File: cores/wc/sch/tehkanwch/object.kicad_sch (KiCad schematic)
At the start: 4 parts

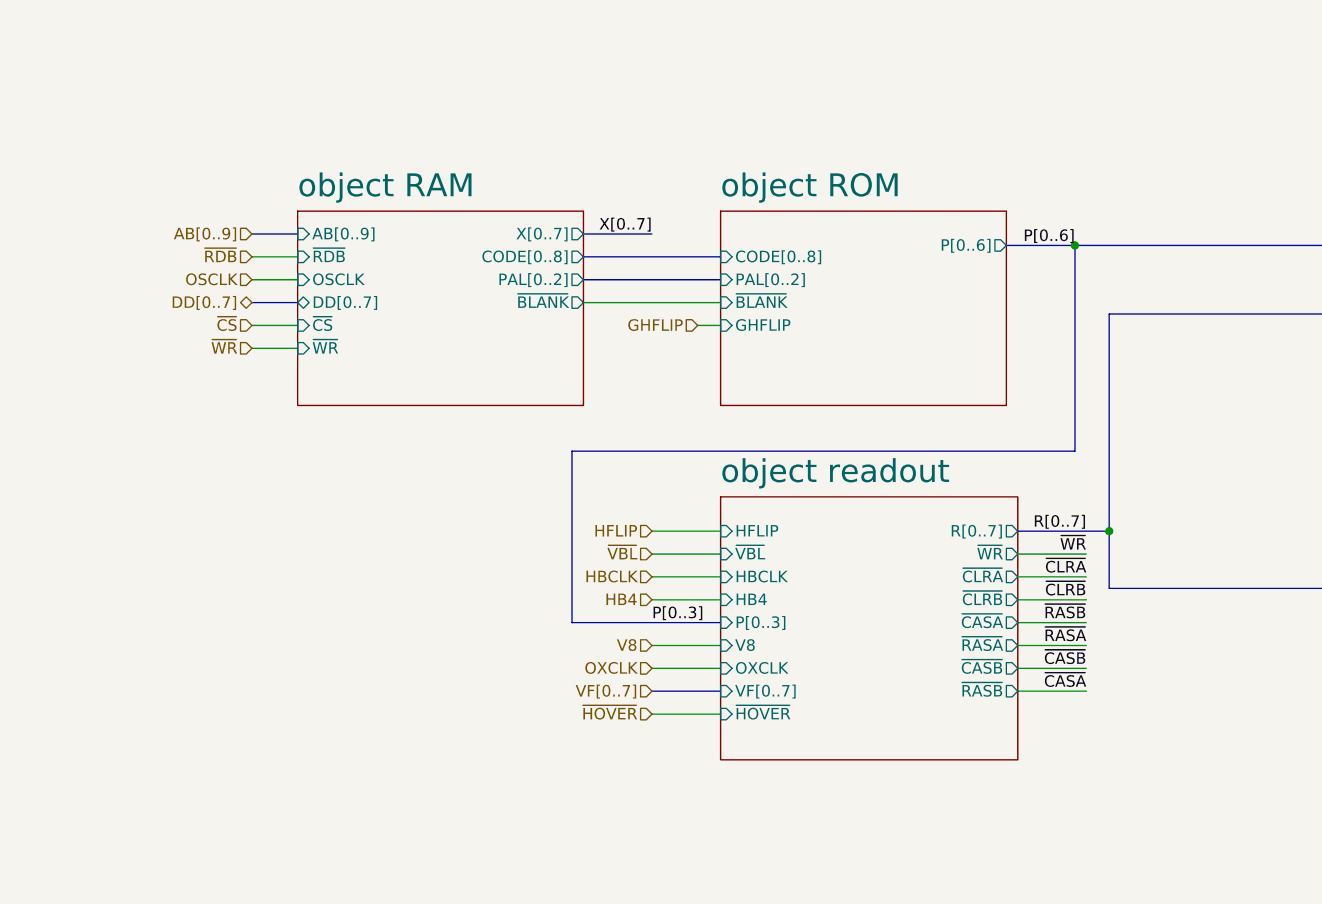
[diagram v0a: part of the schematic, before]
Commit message: wc: all modules connected
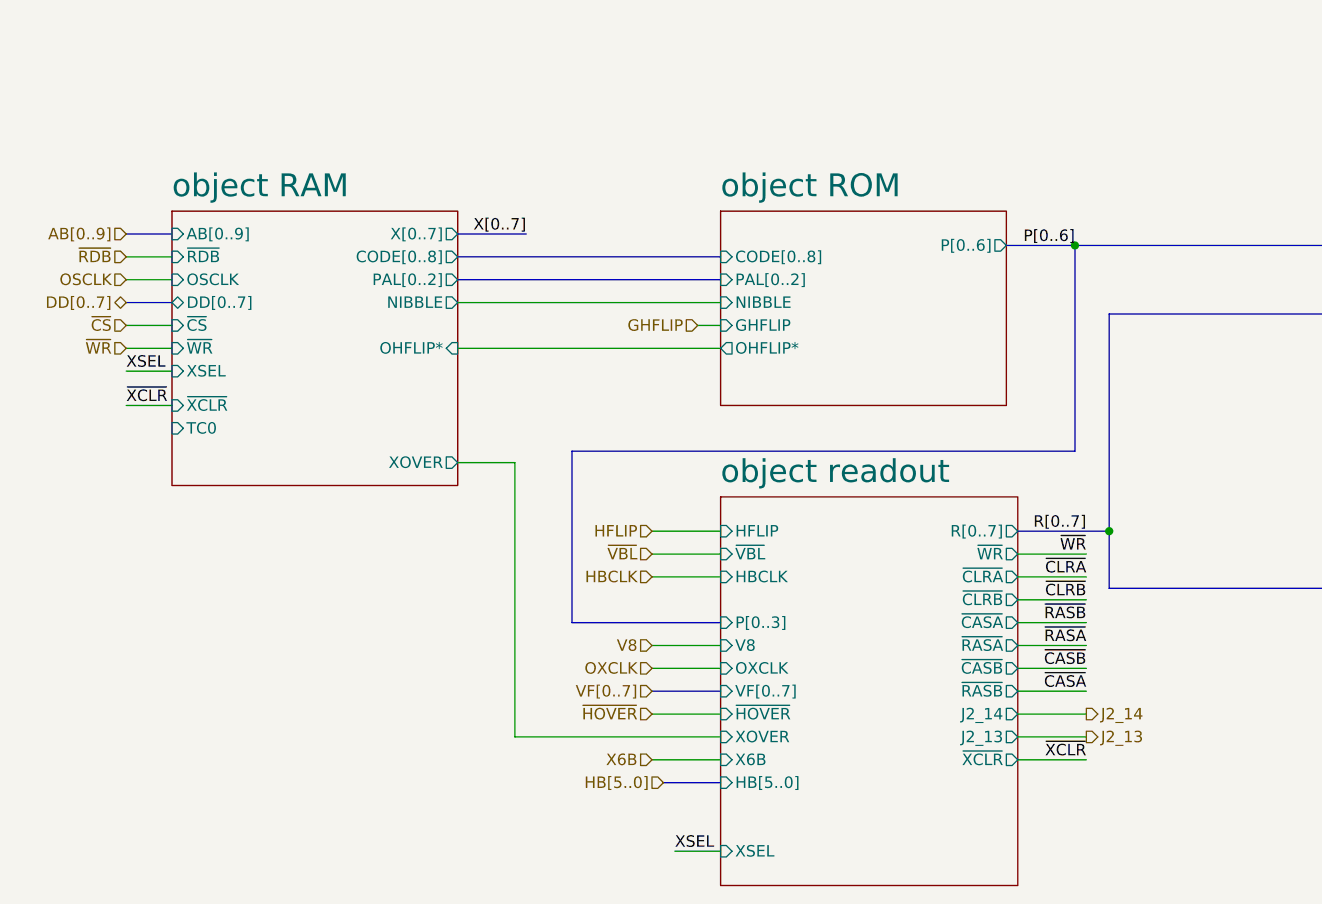
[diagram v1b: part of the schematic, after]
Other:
- sheet object RAM ports: added NIBBLE, OHFLIP*, TC0, XOVER, XSEL, ~{XCLR}; removed ~{BLANK}
- sheet object ROM ports: added NIBBLE, OHFLIP*; removed ~{BLANK}
- sheet object readout ports: added HB[5..0], J2_13, J2_14, X6B, XOVER, XSEL, ~{XCLR}; removed HB4

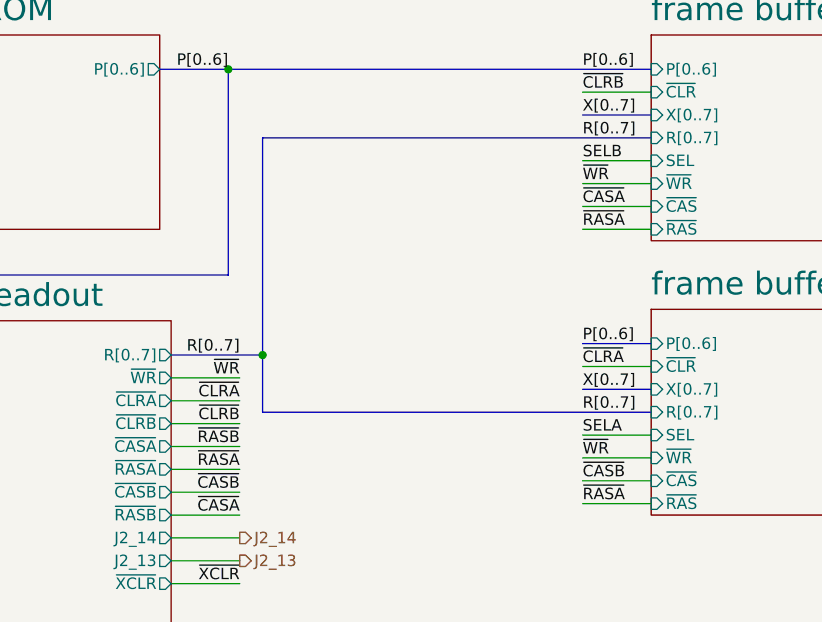
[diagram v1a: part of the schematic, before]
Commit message: wc sch: sub CPU address bus connection to shared memory
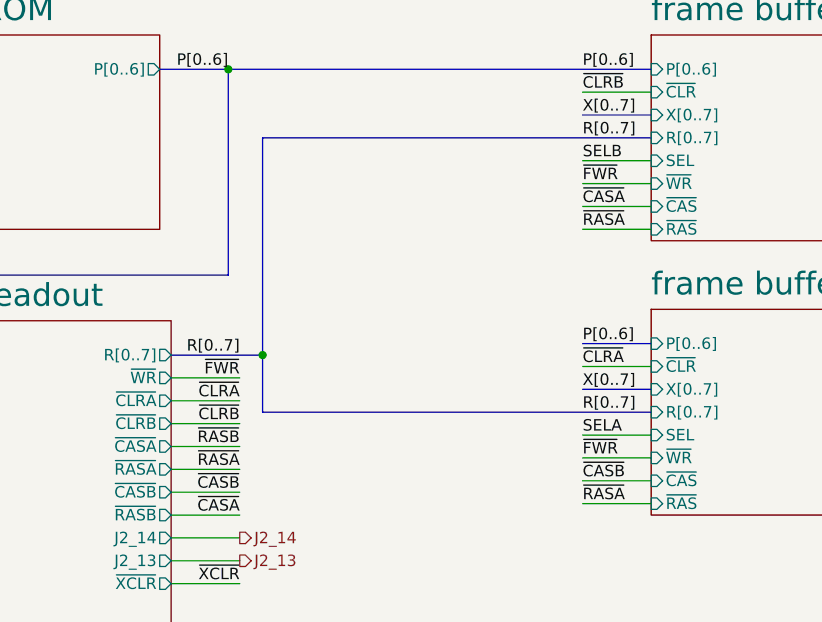
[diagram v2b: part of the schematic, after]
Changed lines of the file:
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@@
 		)
 	)
-	(label "~{WR}"
+	(label "~{FWR}"
 		(at 226.06 130.81 0)
 		(fields_autoplaced yes)
@@
 		)
 	)
-	(label "~{WR}"
+	(label "~{FWR}"
 		(at 226.06 161.29 0)
 		(fields_autoplaced yes)
@@
 		)
 	)
-	(label "~{WR}"
+	(label "~{FWR}"
 		(at 187.96 152.4 180)
 		(fields_autoplaced yes)

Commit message: wc: obj module -wip-
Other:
- sheet object RAM ports: added OCK[0..1], OHFLIP, OVFLIP; removed TC0
- sheet object ROM ports: added OCK[0..1], OHFLIP, OVFLIP; removed none
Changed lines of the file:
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@@
 	(bus
 		(pts
+			(xy 118.11 137.16) (xy 147.32 137.16)
+		)
+		(stroke
+			(width 0)
+			(type default)
+		)
+	)
+	(bus
+		(pts
 			(xy 179.07 118.11) (xy 186.69 118.11)
 		)
@@
 		)
 	)
+	(wire
+		(pts
+			(xy 118.11 134.62) (xy 147.32 134.62)
+		)
+		(stroke
+			(width 0)
+			(type default)
+		)
+	)
 	(bus
 		(pts
@@
 	(wire
 		(pts
+			(xy 118.11 132.08) (xy 147.32 132.08)
+		)
+		(stroke
+			(width 0)
+			(type default)
+		)
+	)
+	(wire
+		(pts
 			(xy 118.11 124.46) (xy 147.32 124.46)
 		)
@@
 	(sheet
 		(at 147.32 114.3)
-		(size 31.75 21.59)
+		(size 31.75 25.4)
 		(fields_autoplaced yes)
 		(stroke
@@
 		)
 		(property "Sheetfile" "objrom.kicad_sch"
-			(at 147.32 136.4746 0)
+			(at 147.32 140.2846 0)
 			(effects
 				(font
@@
 			)
 		)
+		(pin "OHFLIP" input
+			(at 147.32 132.08 180)
+			(effects
+				(font
+					(size 1.27 1.27)
+				)
+				(justify left)
+			)
+		)
+		(pin "OCK[0..1]" input
+			(at 147.32 137.16 180)
+			(effects
+				(font
+					(size 1.27 1.27)
+				)
+				(justify left)
+			)
+		)
+		(pin "OVFLIP" input
+			(at 147.32 134.62 180)
+			(effects
+				(font
+					(size 1.27 1.27)
+				)
+				(justify left)
+			)
+		)
 		(instances
 			(project "tehkanwch"
@@
 			)
 		)
-		(pin "TC0" input
-			(at 86.36 138.43 180)
-			(effects
-				(font
-					(size 1.27 1.27)
-				)
-				(justify left)
-			)
-		)
 		(pin "XSEL" input
 			(at 86.36 132.08 180)
@@
 			(effects
 				(font
+					(size 1.27 1.27)
+				)
+				(justify right)
+			)
+		)
+		(pin "OVFLIP" output
+			(at 118.11 134.62 0)
+			(effects
+				(font
+					(size 1.27 1.27)
+				)
+				(justify right)
+			)
+		)
+		(pin "OHFLIP" output
+			(at 118.11 132.08 0)
+			(effects
+				(font
+					(size 1.27 1.27)
+				)
+				(justify right)
+			)
+		)
+		(pin "OCK[0..1]" output
+			(at 118.11 137.16 0)
+			(effects
+				(font

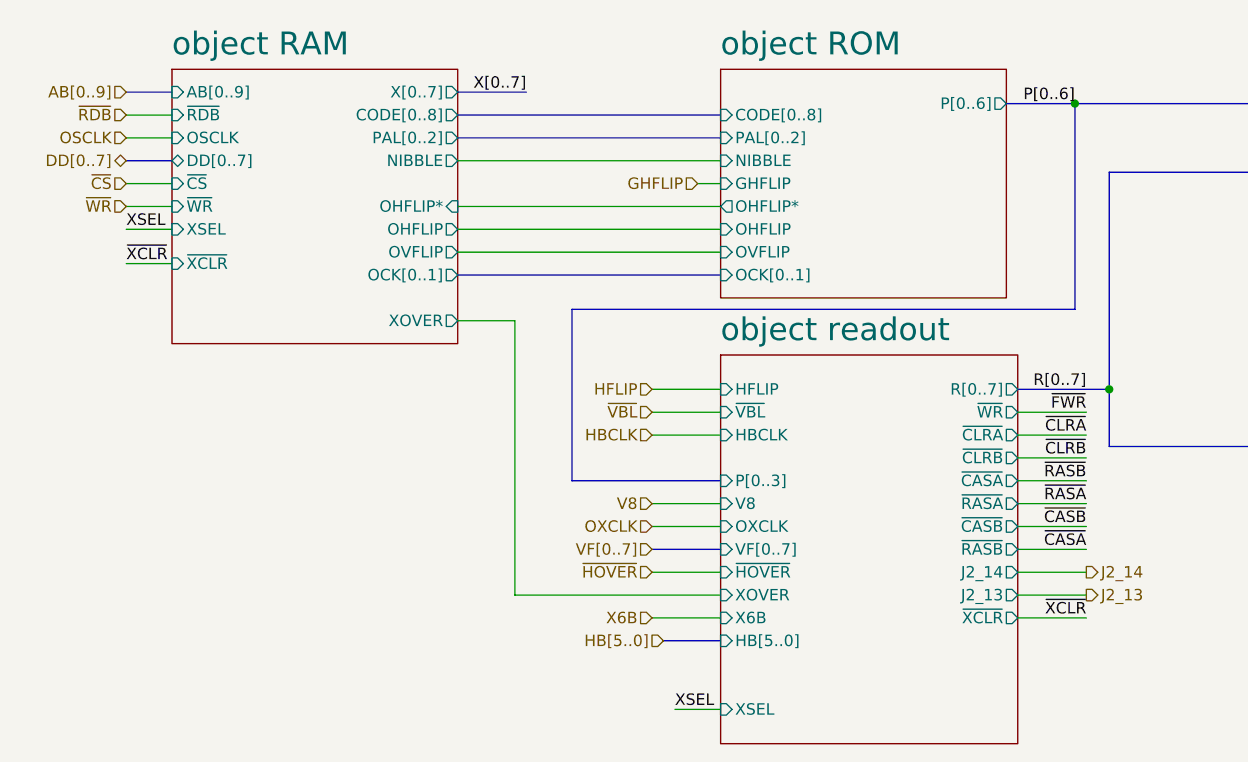
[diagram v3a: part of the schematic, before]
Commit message: wc: playable using tehkanwch controls
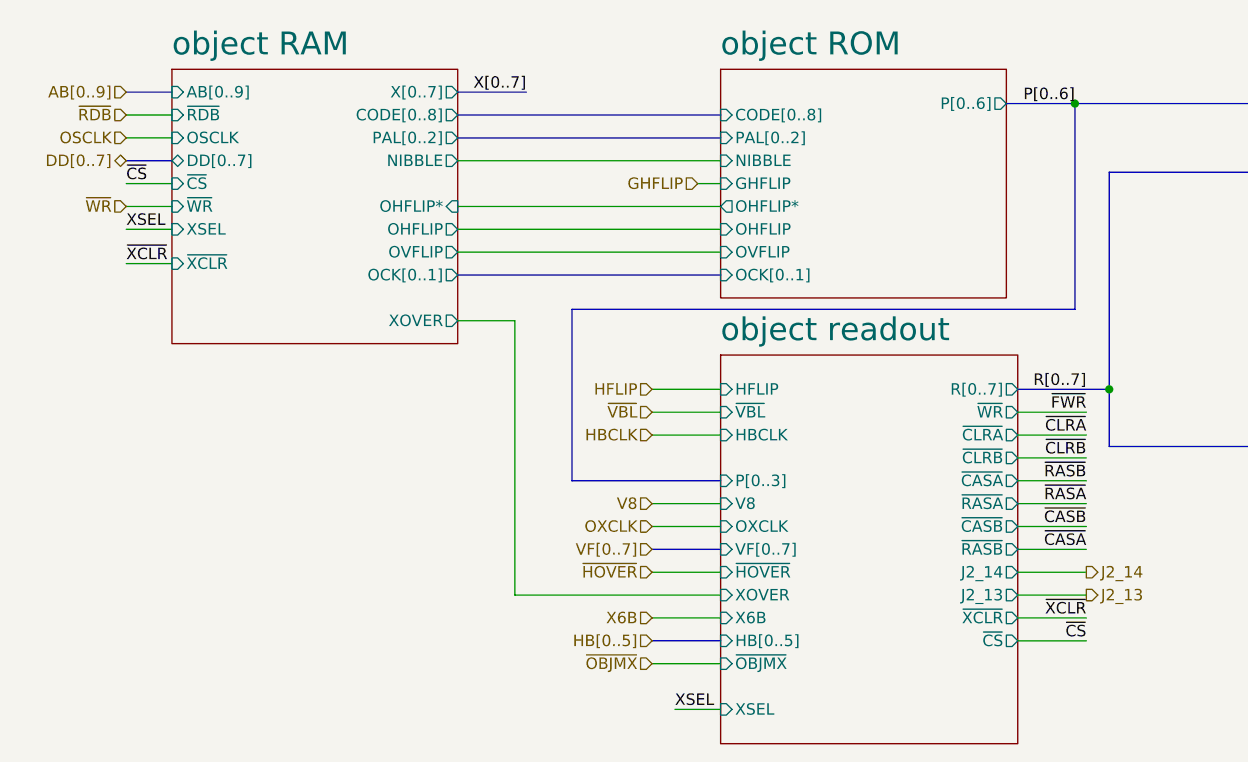
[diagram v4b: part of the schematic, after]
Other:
- sheet object readout ports: added HB[0..5], ~{CS}, ~{OBJMX}; removed HB[5..0]
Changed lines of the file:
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@@
 	(bus
 		(pts
-			(xy 147.32 177.8) (xy 140.97 177.8)
+			(xy 147.32 177.8) (xy 139.7 177.8)
 		)
 		(stroke
@@
 	(wire
 		(pts
+			(xy 139.7 180.34) (xy 147.32 180.34)
+		)
+		(stroke
+			(width 0)
+			(type default)
+		)
+	)
+	(wire
+		(pts
 			(xy 180.34 154.94) (xy 187.96 154.94)
 		)
@@
 	(wire
 		(pts
+			(xy 180.34 177.8) (xy 187.96 177.8)
+		)
+		(stroke
+			(width 0)
+			(type default)
+		)
+	)
+	(wire
+		(pts
 			(xy 139.7 170.18) (xy 147.32 170.18)
 		)
@@
 		)
 	)
+	(label "~{CS}"
+		(at 81.28 127 0)
+		(fields_autoplaced yes)
+		(effects
+			(font
+				(size 1.27 1.27)
+			)
+			(justify left bottom)
+		)
+	)
 	(label "~{FWR}"
 		(at 226.06 130.81 0)
@@
 		)
 	)
+	(label "~{CS}"
+		(at 187.96 177.8 180)
+		(fields_autoplaced yes)
+		(effects
+			(font
+				(size 1.27 1.27)
+			)
+			(justify right bottom)
+		)
+	)
 	(label "R[0..7]"
 		(at 226.06 125.73 0)
@@
 		)
 	)
-	(hierarchical_label "~{CS}"
-		(shape input)
-		(at 81.28 127 180)
-		(fields_autoplaced yes)
-		(effects
-			(font
-				(size 1.27 1.27)
-			)
-			(justify right)
-		)
-	)
 	(hierarchical_label "~{WR}"
 		(shape input)
@@
 		)
 	)
+	(hierarchical_label "~{OBJMX}"
+		(shape input)
+		(at 139.7 180.34 180)
+		(fields_autoplaced yes)
+		(effects
+			(font
+				(size 1.27 1.27)
+			)
+			(justify right)
+		)
+	)
 	(hierarchical_label "VF[0..7]"
 		(shape input)
@@
 		)
 	)
+	(hierarchical_label "HB[0..5]"
+		(shape input)
+		(at 139.7 177.8 180)
+		(fields_autoplaced yes)
+		(effects
+			(font
+				(size 1.27 1.27)
+			)
+			(justify right)
+		)
+	)
 	(hierarchical_label "X6B"
 		(shape input)
@@
 		)
 	)
-	(hierarchical_label "HB[5..0]"
-		(shape input)
-		(at 140.97 177.8 180)
-		(fields_autoplaced yes)
-		(effects
-			(font
-				(size 1.27 1.27)
-			)
-			(justify right)
-		)
-	)
 	(symbol
 		(lib_id "Device:R_Network08_US")
@@
 			)
 		)
-		(pin "HB[5..0]" input
+		(pin "HB[0..5]" input
 			(at 147.32 177.8 180)
 			(effects
@@
 			)
 		)
+		(pin "~{CS}" output
+			(at 180.34 177.8 0)
+			(effects
+				(font
+					(size 1.27 1.27)
+				)
+				(justify right)
+			)
+		)
+		(pin "~{OBJMX}" input
+			(at 147.32 180.34 180)
+			(effects
+				(font
+					(size 1.27 1.27)
+				)
+				(justify left)
+			)
+		)

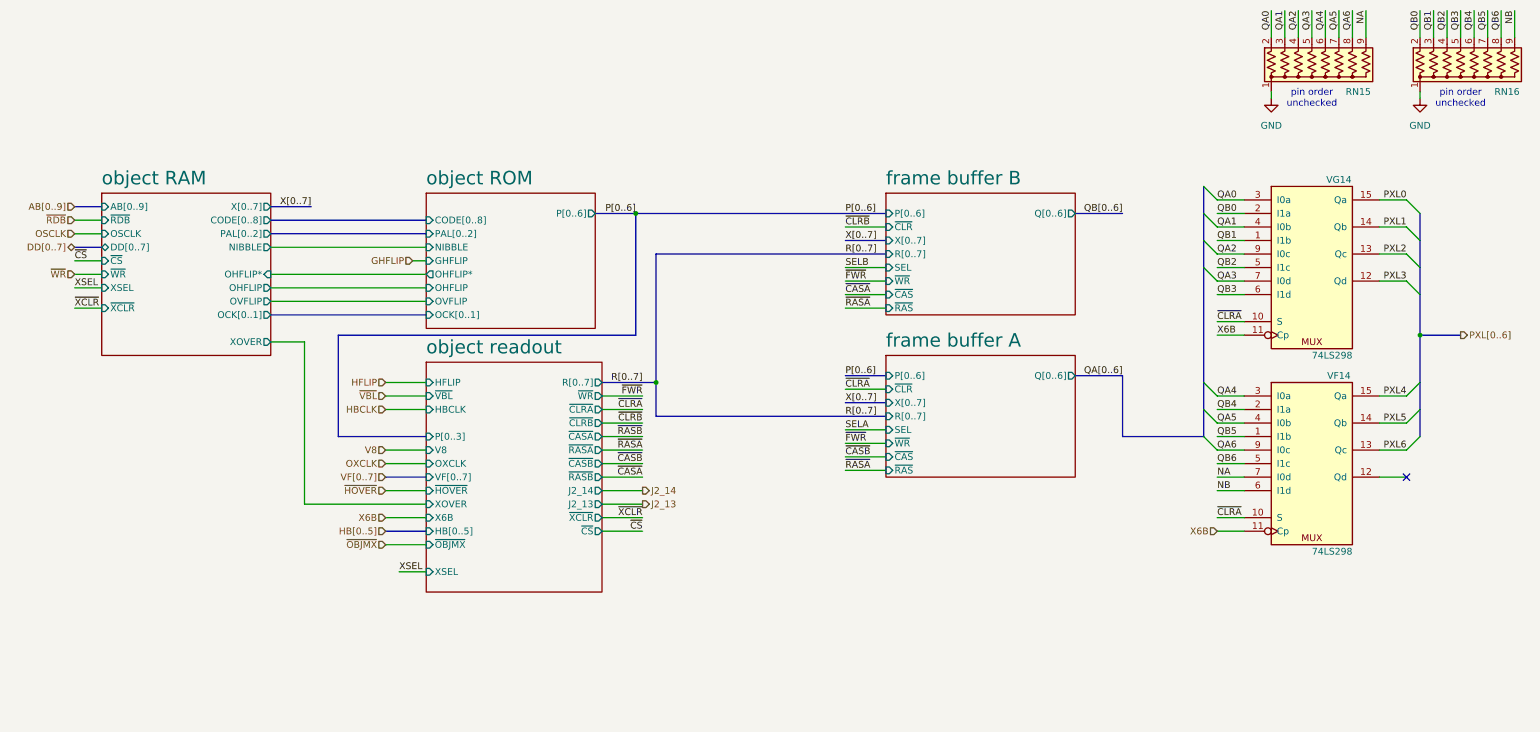
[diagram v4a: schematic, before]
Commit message: wc: support for analog gamepad
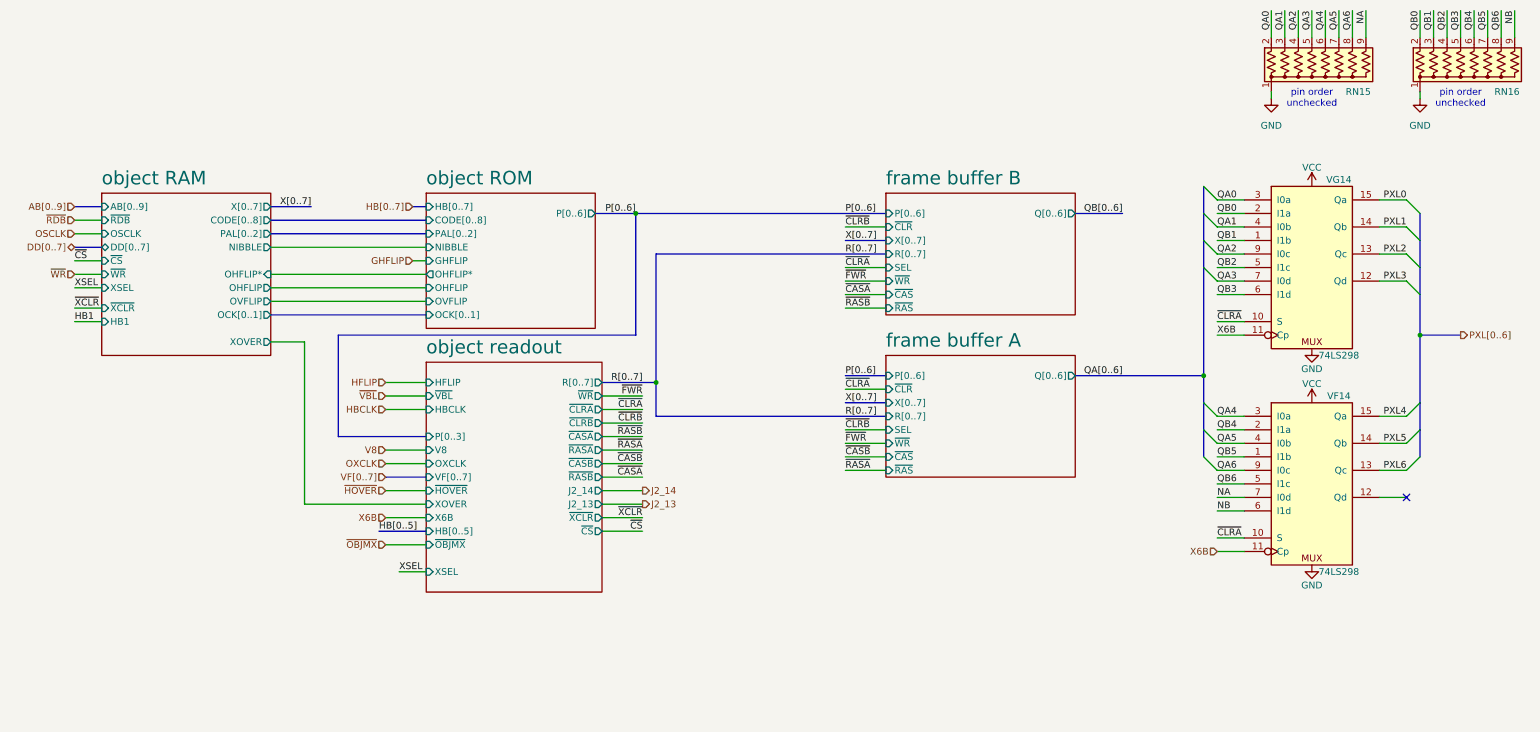
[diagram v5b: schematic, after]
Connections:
- net VSS is gone; now on net GND: VF14.8 (VSS), VG14.8 (VSS)
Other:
- sheet object RAM ports: added HB1; removed none
- sheet object ROM ports: added HB[0..7]; removed none
- moved on the sheet: VF14

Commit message: sch
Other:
- sheet object readout ports: added ~{CSSET}; removed none
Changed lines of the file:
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@@
+	(wire
+		(pts
+			(xy 180.34 180.34) (xy 187.96 180.34)
+		)
+		(stroke
+			(width 0)
+			(type default)
+		)
+	)
 	(wire
 		(pts
@@
 			)
 			(justify right)
+		)
+	)
+	(hierarchical_label "~{CSSET}"
+		(shape output)
+		(at 187.96 180.34 0)
+		(fields_autoplaced yes)
+		(effects
+			(font
+				(size 1.27 1.27)
+			)
+			(justify left)
 		)
 	)
@@
 			)
 		)
+		(pin "~{CSSET}" output
+			(at 180.34 180.34 0)
+			(effects
+				(font
+					(size 1.27 1.27)
+				)
+				(justify right)
+			)
+		)

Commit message: wc: tehkanwch sch
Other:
- sheet object RAM ports: added ~{ATTR}, ~{CODE}; removed none
- sheet object ROM ports: added ~{HB1}, ~{PALCP}; removed GHFLIP
- sheet object readout ports: added HB[0..6], OCK[0..1], ~{ATTR}, ~{CODE}, ~{HB1}, ~{PALCP}, ~{Y6}*; removed HB[0..5]
